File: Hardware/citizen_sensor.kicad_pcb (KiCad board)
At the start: 2 copper layers, 64 parts, among them J1 BATT, J2 USB_B_Micro, J3 VEML6075, J4 BME280, J5 PROG, J6 CSS811, J7 MAX30105, Q1 2N7002, SW1 RST, U1 TLC2272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

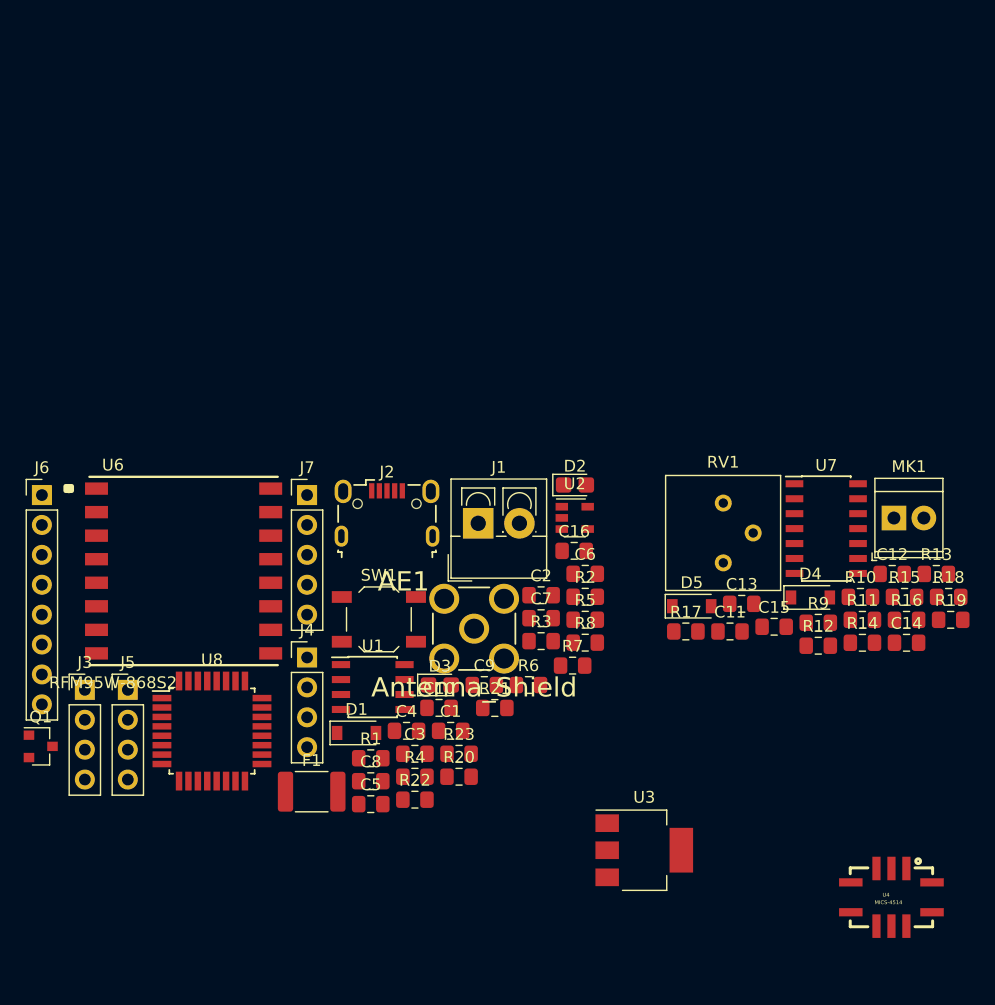
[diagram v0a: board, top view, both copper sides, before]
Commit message: PCB routed 0.1v
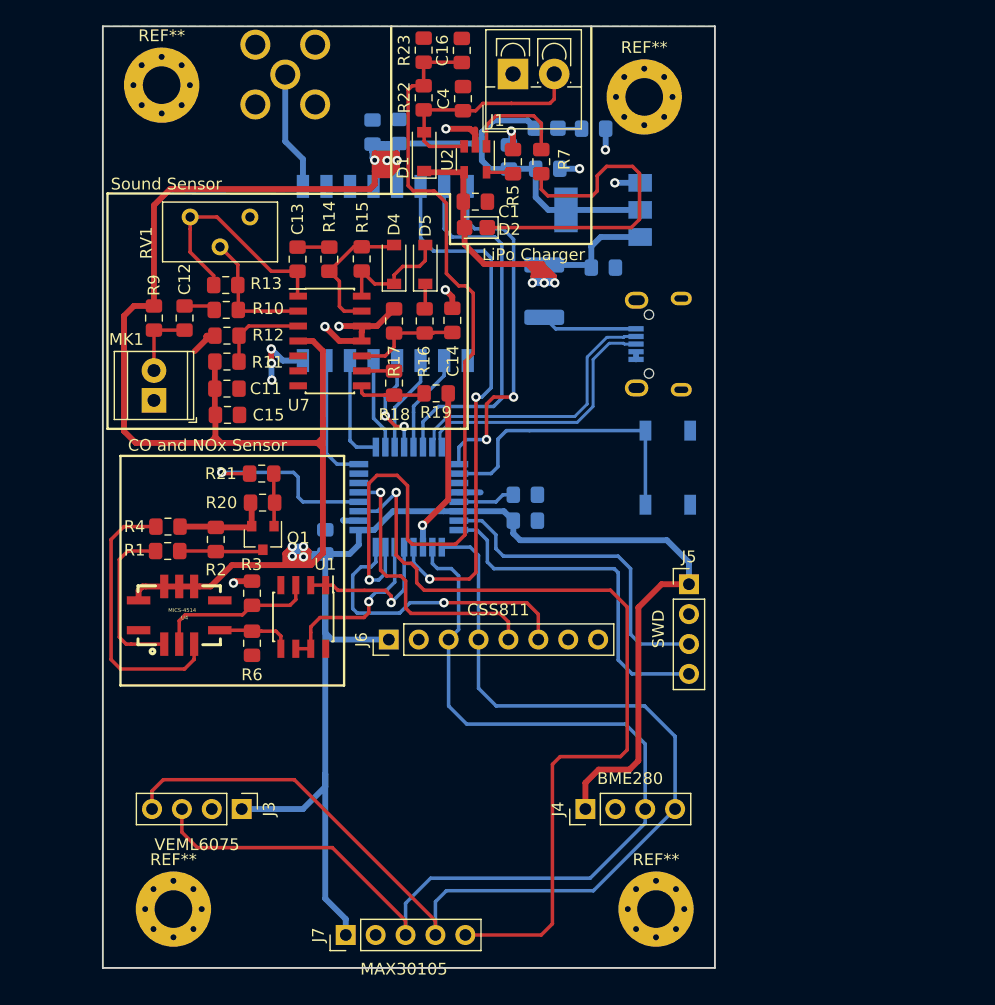
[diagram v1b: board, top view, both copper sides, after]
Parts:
- added REF**: MountingHole_3.2mm_M3_Pad_Via, MountingHole:MountingHole_3.2mm_M3_Pad_Via, F.Cu at (171.0, 115.0)
- added REF**: MountingHole_3.2mm_M3_Pad_Via, MountingHole:MountingHole_3.2mm_M3_Pad_Via, F.Cu at (130.0, 115.0)
- added REF**: MountingHole_3.2mm_M3_Pad_Via, MountingHole:MountingHole_3.2mm_M3_Pad_Via, F.Cu at (129.0, 45.0)
- added REF**: MountingHole_3.2mm_M3_Pad_Via, MountingHole:MountingHole_3.2mm_M3_Pad_Via, F.Cu at (170.0, 46.0)
- AE1, C10, C2, C3, C5, C6, C7, C8, C9, D3, F1, J2, R8, SW1, U3, U6, U8: moved to B.Cu
- RV1: footprint Potentiometer_THT:Potentiometer_Bourns_3386P_Vertical -> Potentiometer_THT:Potentiometer_Bourns_3386X_Horizontal
- moved R13 65.2 mm to (134.4, 62.0), turned to 180 degrees
- moved U4 65.1 mm to (130.5, 90.0), turned to 180 degrees
- moved C12 63.9 mm to (130.9, 64.8), turned to 90 degrees
- moved MK1 63.7 mm to (128.3, 71.8), turned to 90 degrees
- moved R9 62.1 mm to (128.3, 64.8), turned to 270 degrees
- moved R23 59.9 mm to (151.3, 42.0), turned to 270 degrees
- moved R22 59.6 mm to (151.3, 46.1), turned to 270 degrees
- moved R10 59.1 mm to (134.5, 64.1), turned to 180 degrees
- moved R11 58.3 mm to (134.5, 68.5)
- moved R12 56.7 mm to (134.5, 66.3)
- moved C5 56.0 mm to (161.8, 52.1)
- moved R14 55.8 mm to (143.2, 59.8), turned to 90 degrees
- moved U3 54.5 mm to (166.5, 55.6), turned to 180 degrees
- moved R15 54.3 mm to (146.0, 59.8), turned to 90 degrees
- moved C4 53.9 mm to (154.6, 46.1), turned to 90 degrees
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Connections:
- U7 pad 10: (no net) -> Net-(C14-Pad2)
- U7 pad 12: Net-(C14-Pad2) -> GND
- U7 pad 13: Net-(R18-Pad1) -> Net-(D4-Pad2)
- U7 pad 14: Net-(R18-Pad2) -> Net-(D4-Pad1)
- U7 pad 5: GND -> (no net)
- U7 pad 6: Net-(D4-Pad2) -> (no net)
- U7 pad 7: Net-(D4-Pad1) -> (no net)
- U7 pad 8: (no net) -> Net-(R18-Pad2)
- U7 pad 9: (no net) -> Net-(R18-Pad1)
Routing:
- net +3V3: track 0.00 -> 311.5 mm, vias 0 -> 7
- net /SDA: track 0.00 -> 97.9 mm
- net /SCL: track 0.00 -> 91.4 mm
- net /BATTLEVEL: track 0.00 -> 74.4 mm, vias 0 -> 1
- net /INT: track 0.00 -> 71.7 mm, vias 0 -> 1
- net VCC: track 0.00 -> 63.1 mm, vias 0 -> 3
- net GND: track 0.00 -> 47.6 mm, vias 0 -> 12
- net /DIO0: track 0.00 -> 46.1 mm, vias 0 -> 2
- net /DIO1: track 0.00 -> 31.8 mm
- net /DIO2: track 0.00 -> 30.5 mm, vias 0 -> 2
- net /SWDIO: track 0.00 -> 30.0 mm
- net Net-(D2-Pad1): track 0.00 -> 29.1 mm
- net /SWCLK: track 0.00 -> 27.9 mm
- net /INTCSS: track 0.00 -> 25.4 mm, vias 0 -> 1
- net Net-(SW1-Pad2): track 0.00 -> 25.0 mm
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- added copper zone on B.Cu, net GND
- added copper zone on F.Cu, net GND
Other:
- board outline added: 52 x 80 mm
- net class Default: clearance 0.2 -> 0.25; trace_width 0.25 -> 0.3
- net class vcc added: clearance 0.25, trace_width 0.5, via_dia 0.8, via_drill 0.4
- rule trace_clearance: 0.2 -> 0.25
- board text added: "3.3v"
- board text added: "CO and NOx Sensor"
- board text added: "GND"
- board text added: "LiPo Charger"
- board text added: "SWCLK"
- board text added: "SWD"
- board text added: "SWDIO"
- board text added: "Sound Sensor"

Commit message: add logos
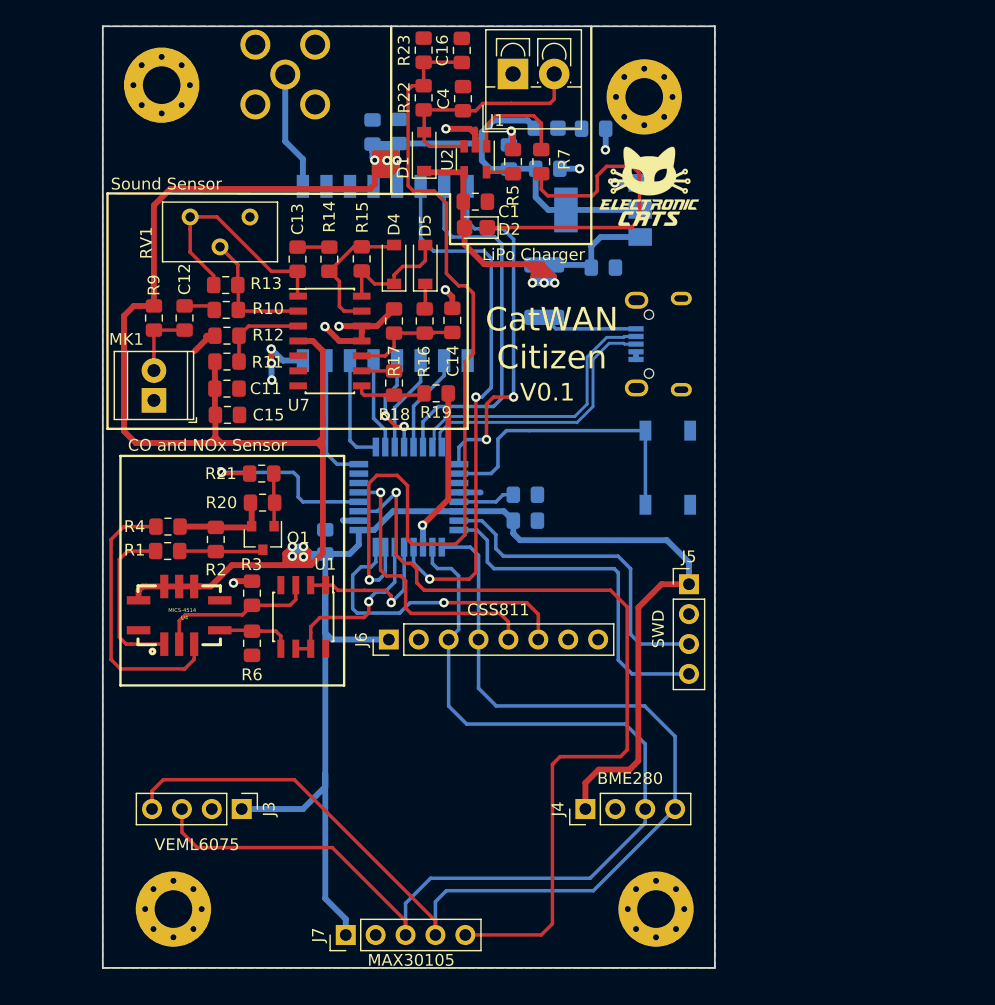
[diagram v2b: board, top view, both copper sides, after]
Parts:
- added G***: LOGO, Aesthetics:electronic_cats_logo_8x6, F.Cu at (170.4, 53.6)
- added G***: LOGO, Aesthetics:electronic_cats_logo_8x6, B.Cu at (133.0, 80.6)
- added REF***: WEEE-Logo_4.2x6mm_SilkScreen, Symbols:WEEE-Logo_4.2x6mm_SilkScreen, B.Cu at (144.8, 104.7)
- added REF***: OSHW-Logo_7.5x8mm_SilkScreen, Symbols:OSHW-Logo_7.5x8mm_SilkScreen, B.Cu at (155.9, 105.0)
- U6: value RFM95W-868S2 -> RFM95
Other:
- board text added: "CatWAN Citizen"
- board text added: "V0.1"
- board text added: "v0.1"

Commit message: add logo fablab yucatan ♥️
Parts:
- added G***: LOGO, Aesthetics:fablab_yucatan, F.Cu at (170.7, 56.7)
- added G***: LOGO, Aesthetics:fablab_yucatan, B.Cu at (161.9, 99.1)
- REF*** (x2): moved to F.Cu
- moved G*** 24.2 mm to (171.2, 77.8)
- moved G*** 18.0 mm to (138.0, 97.9)
- moved REF*** 13.5 mm to (136.8, 115.6), turned to 0 degrees
- moved REF*** 11.9 mm to (163.2, 114.4), turned to 0 degrees

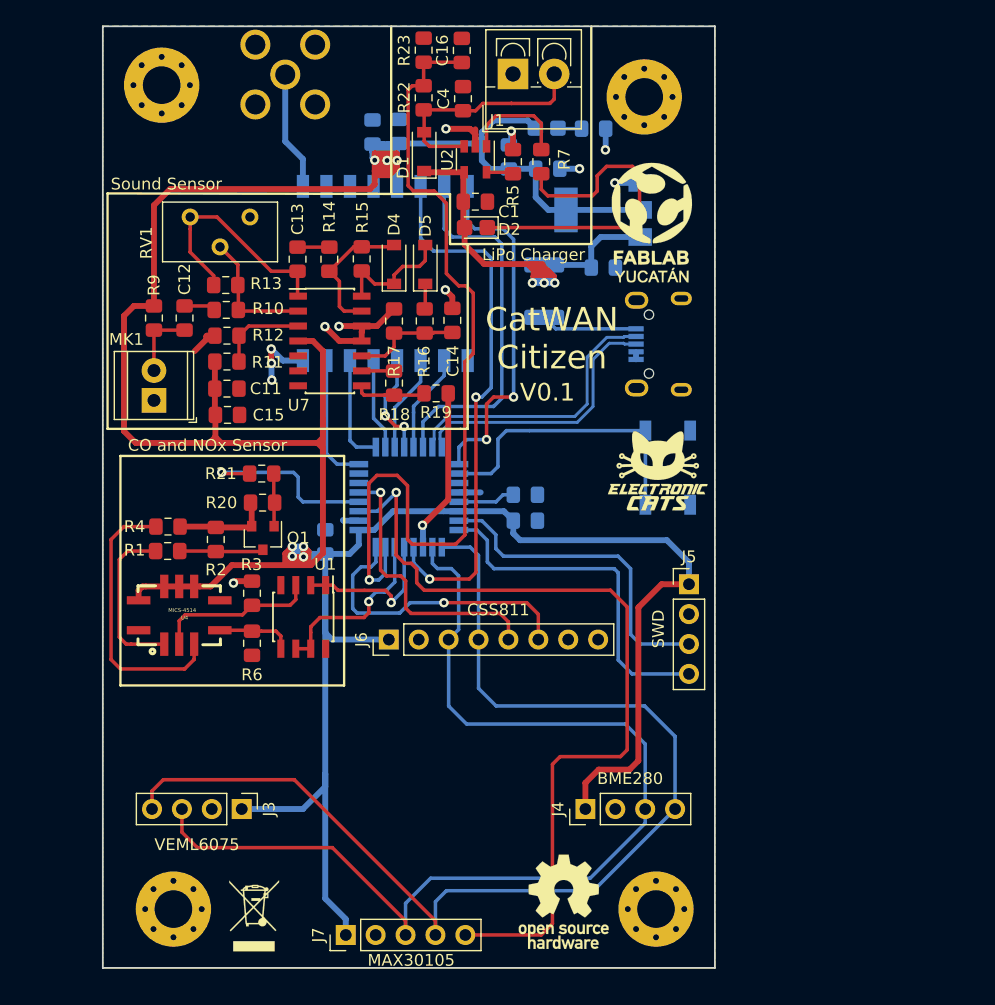
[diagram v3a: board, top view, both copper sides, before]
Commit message: Fix antenna and mounting holes
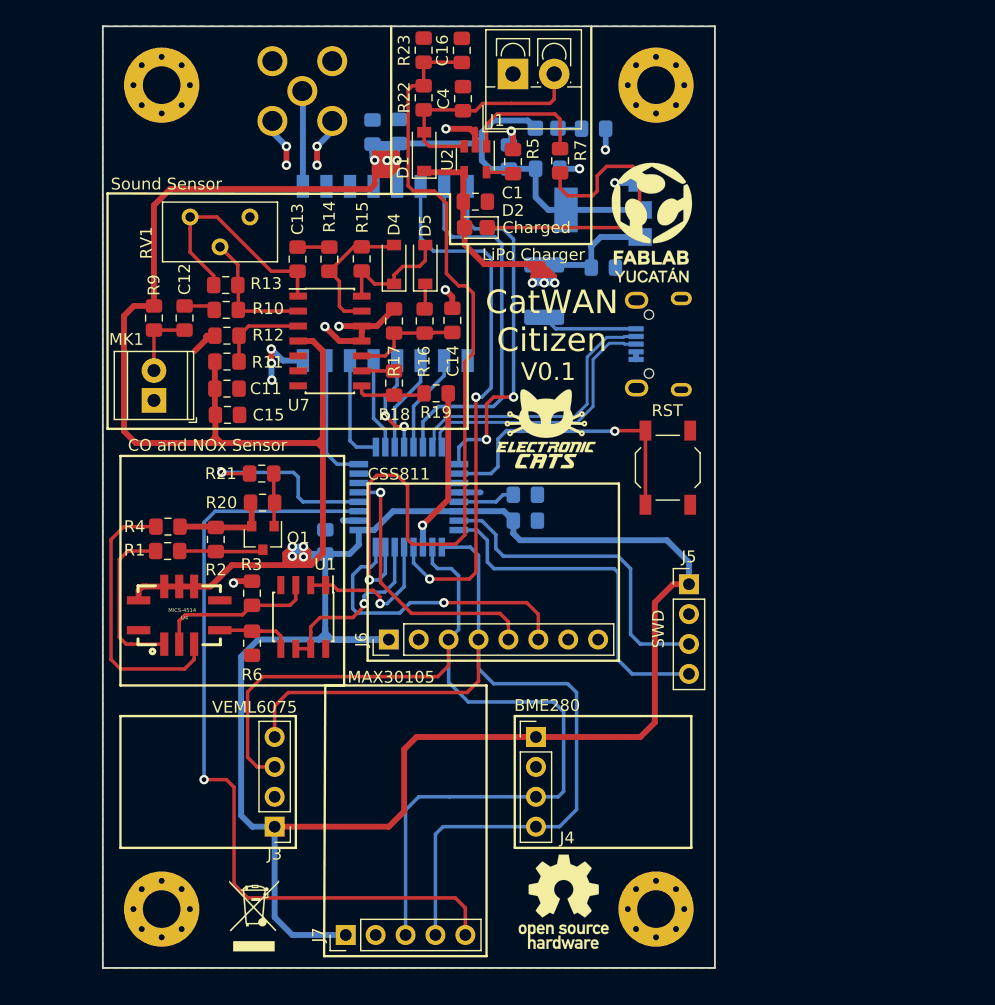
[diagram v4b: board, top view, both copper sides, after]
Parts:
- SW1: moved to F.Cu
- moved G*** 10.2 mm to (161.7, 74.2)
- moved J4 7.42 mm to (160.8, 100.4), turned to 0 degrees
- moved J3 3.18 mm to (138.6, 108.0), turned to 180 degrees
- moved AE1 2.02 mm to (140.9, 45.5)
- moved R7 1.60 mm to (162.8, 51.4)
- moved REF** 1.41 mm to (171.0, 45.0)
- moved REF** 1.00 mm to (129.0, 115.0)
- turned SW1 to 270 degrees
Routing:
- net +3V3: track 311.5 -> 345.6 mm
- net /SDA: track 97.9 -> 77.9 mm
- net GND: track 47.6 -> 56.2 mm, vias 12 -> 16
- net /SCL: track 91.4 -> 84.1 mm
- net /INT: track 71.7 -> 69.2 mm
- net Net-(SW1-Pad2): track 25.0 -> 27.0 mm, vias 0 -> 1
- net Net-(AE1-Pad1): track 10.1 -> 8.12 mm
- net Net-(R7-Pad1): track 9.28 -> 11.2 mm
- net Net-(D2-Pad1): track 29.1 -> 27.5 mm
- net /WAKE: track 24.0 -> 23.2 mm
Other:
- board text added: "Charged"

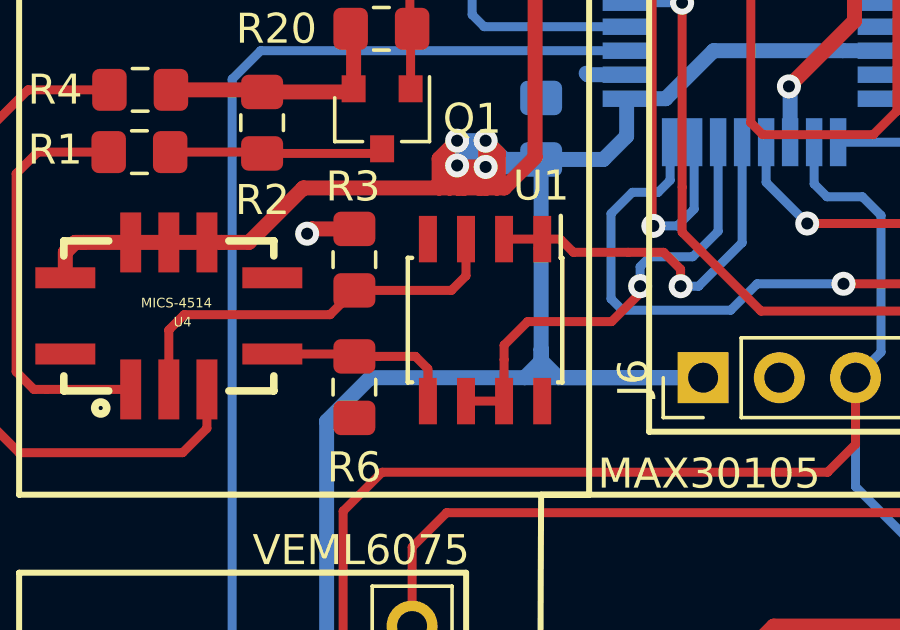
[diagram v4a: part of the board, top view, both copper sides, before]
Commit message: fix VDD y GND of TLC2272
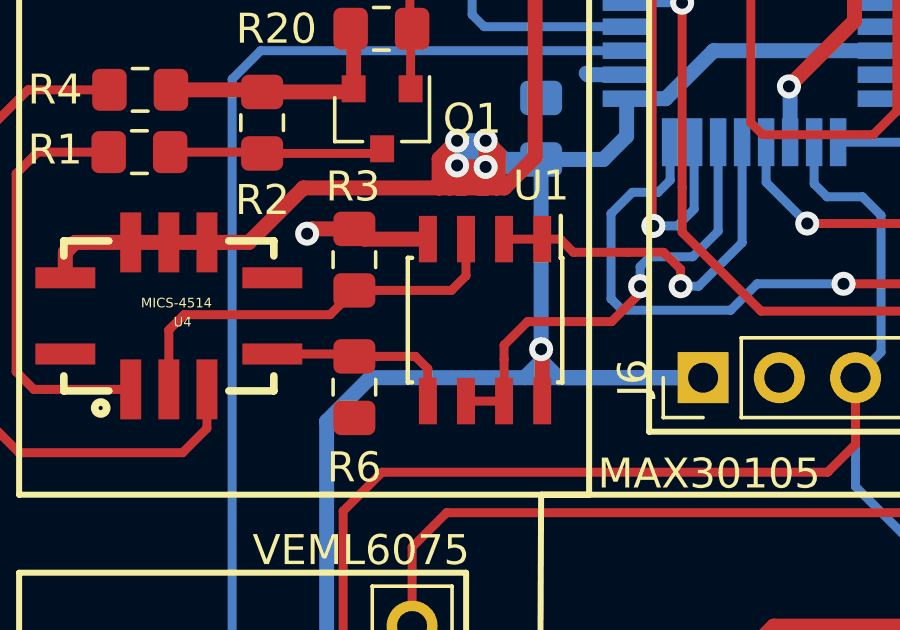
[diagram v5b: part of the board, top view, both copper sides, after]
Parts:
- U6: value RFM95 -> RFM95W-868S2
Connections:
- U1 pad 4: (no net) -> GND
- U1 pad 8: (no net) -> +3V3
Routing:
- net GND: track 56.2 -> 58.8 mm
- net +3V3: track 345.6 -> 347.4 mm, vias 7 -> 8
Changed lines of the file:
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@@
-(kicad_pcb (version 20171130) (host pcbnew "(5.0.1-3-g963ef8bb5)")
+(kicad_pcb (version 20171130) (host pcbnew "(5.0.2)-1")
   (general
     (thickness 1.6)
     (drawings 49)
-    (tracks 743)
+    (tracks 748)
     (zones 0)
     (modules 74)
@@
     (solder_mask_min_width 0.25)
     (aux_axis_origin 0 0)
-    (visible_elements FFFFFF7F)
+    (visible_elements 7FFFFFFF)
     (pcbplotparams
       (layerselection 0x010fc_ffffffff)
@@
       (effects (font (size 1 1) (thickness 0.15)))
     )
-    (pad 8 smd rect (at 2.7 -1.905 270) (size 1.55 0.6) (layers F.Cu F.Paste F.Mask))
+    (pad 8 smd rect (at 2.7 -1.905 270) (size 1.55 0.6) (layers F.Cu F.Paste F.Mask)
+      (net 4 +3V3))
     (pad 7 smd rect (at 2.7 -0.635 270) (size 1.55 0.6) (layers F.Cu F.Paste F.Mask)
       (net 46 /ADC_RED))
@@
     (pad 5 smd rect (at 2.7 1.905 270) (size 1.55 0.6) (layers F.Cu F.Paste F.Mask)
       (net 35 /CO2))
-    (pad 4 smd rect (at -2.7 1.905 270) (size 1.55 0.6) (layers F.Cu F.Paste F.Mask))
+    (pad 4 smd rect (at -2.7 1.905 270) (size 1.55 0.6) (layers F.Cu F.Paste F.Mask)
+      (net 2 GND))
     (pad 3 smd rect (at -2.7 0.635 270) (size 1.55 0.6) (layers F.Cu F.Paste F.Mask)
       (net 32 /NO2))
@@
       (effects (font (size 1 1) (thickness 0.15)) (justify mirror))
     )
-    (fp_text value RFM95 (at -6 -9.49147 90) (layer B.SilkS)
+    (fp_text value RFM95W-868S2 (at -6 -9.49147 90) (layer B.SilkS)
       (effects (font (size 1 1) (thickness 0.15)) (justify mirror))
     )
@@
   (via (at 142.2 51.8) (size 0.8) (drill 0.4) (layers F.Cu B.Cu) (net 2))
   (segment (start 142.2 50.2) (end 142.2 51.8) (width 0.5) (layer F.Cu) (net 2))
+  (segment (start 137.015 87.48) (end 136.675 87.14) (width 0.5) (layer F.Cu) (net 2))
+  (segment (start 139.125 87.48) (end 137.015 87.48) (width 0.5) (layer F.Cu) (net 2))
   (via (at 161.5 61.8) (size 0.8) (drill 0.4) (layers F.Cu B.Cu) (net 3))
   (segment (start 161.5 61.3) (end 161.5 61.8) (width 0.3) (layer F.Cu) (net 3))
@@
   (segment (start 135.75 93.55) (end 137.2 92.1) (width 0.5) (layer B.Cu) (net 4))
   (segment (start 135.75 107.05) (end 135.75 93.55) (width 0.5) (layer B.Cu) (net 4))
+  (via (at 142.9 91.15) (size 0.8) (drill 0.4) (layers F.Cu B.Cu) (net 4))
+  (segment (start 142.935 92.88) (end 142.935 91.185) (width 0.5) (layer F.Cu) (net 4))
+  (segment (start 142.935 91.185) (end 142.9 91.15) (width 0.5) (layer F.Cu) (net 4))
   (segment (start 154.525 47.1) (end 154.6 47.175) (width 0.3) (layer F.Cu) (net 5))
   (segment (start 151.258995 47.1) (end 154.525 47.1) (width 0.3) (layer F.Cu) (net 5))
